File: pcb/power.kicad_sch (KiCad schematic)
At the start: 8 parts, among them Q1 AO3400A, Q2 AO3400A, U1 LM74610, U2 LM74610

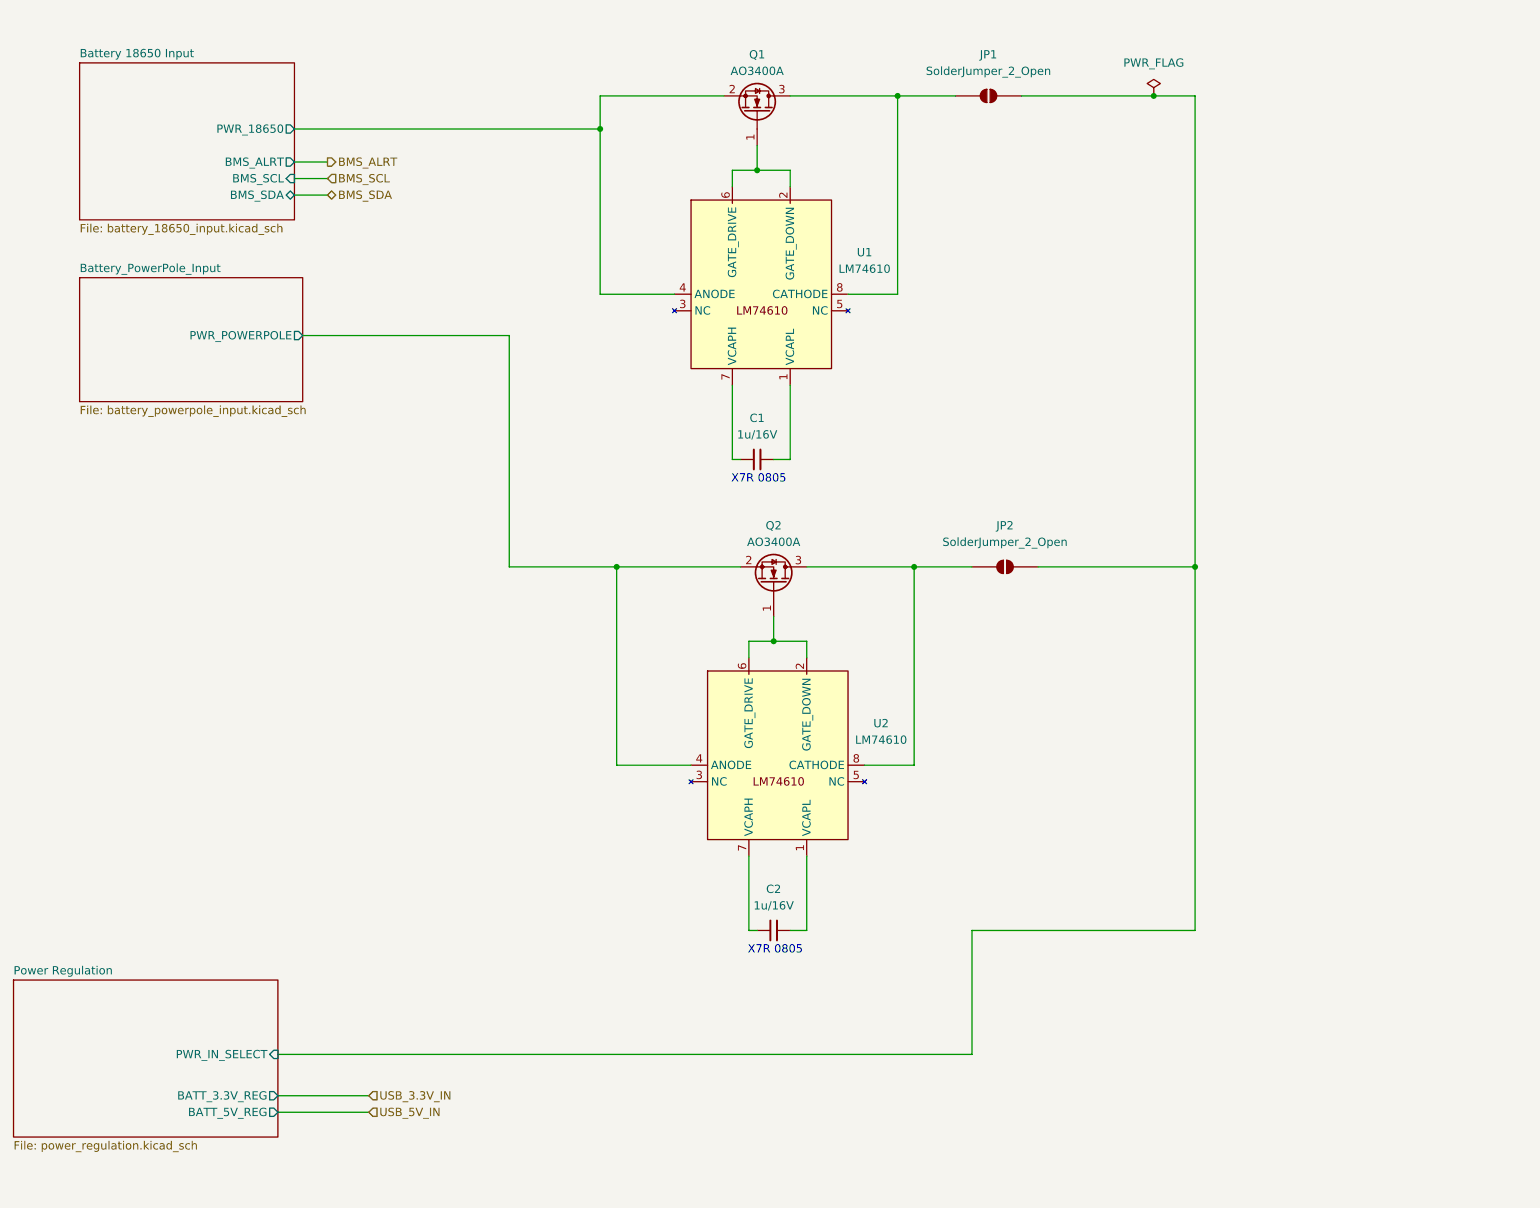
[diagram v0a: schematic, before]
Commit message: Replace battery/PowerPole ORing FETs with TPS2121 in VCOMP mode
power.kicad_sch: U12 (TPS2121RUXR) replaces the two LM74610+AO3400A ideal-
diode branches, configured per TI's "Highest Voltage Operation" (VCOMP,
Fig 10-15): PR1/CP2 tied to GND, OV1/OV2 resistor dividers (23.7k/5k) off
IN1 (PWR_18650) and IN2 (PWR_POWERPOLE), ILM set via R24 (51.1k), SS
ramped through C39 (0.01uF), ST tied directly to GND (unused). Divider
topology, ILM, and SS/ST wiring were each wrong on the first pass and
have been traced pin-by-pin and verified correct against the reference
schematic.

usbc-programming-uart.kicad_sch: CH340C VCC/V3 pin fix (VCC now correctly
powered from VBUS, V3 no longer driven externally) and F3 polyfuse
(16V/500mA) added in series on VBUS upstream of the hub/CH340/AMS1117.

battery_18650_input.kicad_sch, foxhunt1.kicad_pro: incidental KiCad
save cleanup (unused symbol-cache entry pruned, two collinear wire
segments merged, designator bookkeeping reordered) -- no circuit changes.

Bumps kicad_gx_library for the new TPS2121RUXR part. Adds
_docs/hardware/usb_battery_power_mux.md documenting the planned
3-stage TPS2121 architecture (this commit implements stage 1; stages
2/3, the USB-vs-regulator muxes, are not yet implemented).

Co-Authored-By: Claude Sonnet 5 <noreply@anthropic.com>
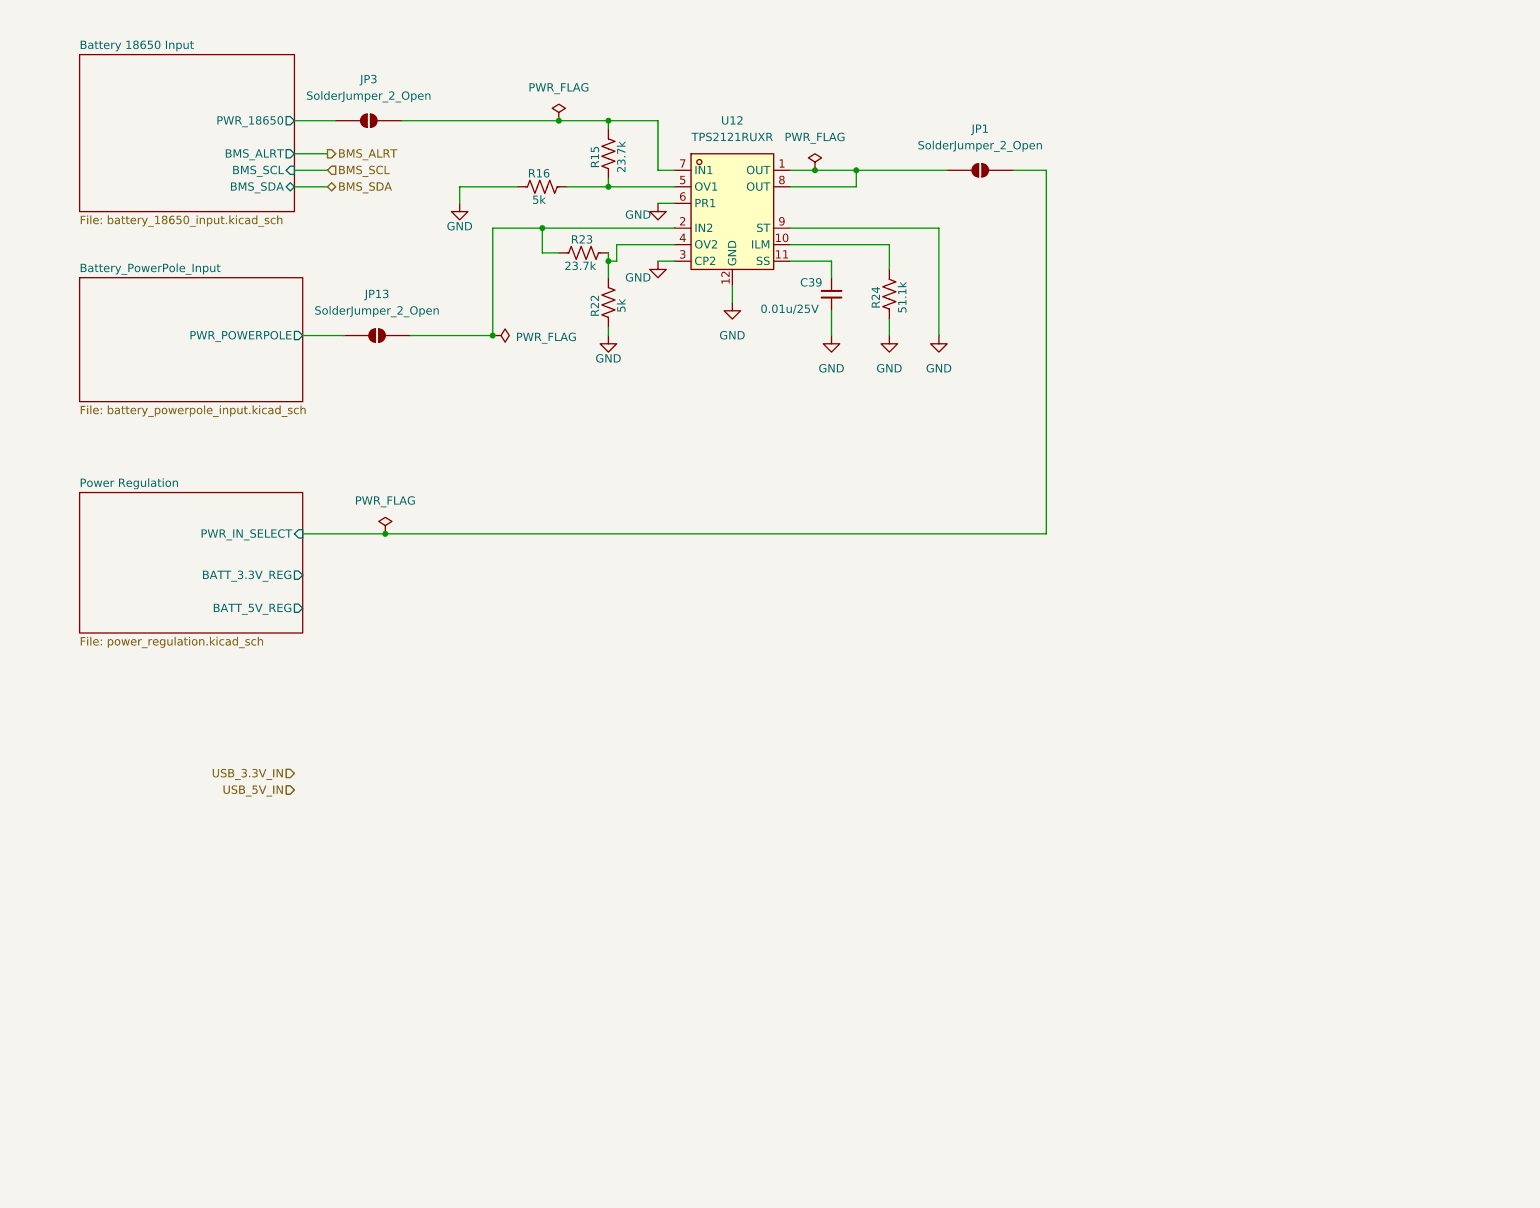
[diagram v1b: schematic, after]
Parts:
- removed C1, C2: 1u/16V, Capacitor_SMD:C_0805_2012Metric, symbol Device:C_Small
- removed JP2: SolderJumper_2_Open, Jumper:SolderJumper-2_P1.3mm_Open_TrianglePad1.0x1.5mm, symbol Jumper:SolderJumper_2_Open
- removed Q1, Q2: AO3400A, Package_TO_SOT_SMD:SOT-23, symbol Transistor_FET:AO3400A
- removed U1, U2: LM74610, Package_SO:VSSOP-8_3x3mm_P0.65mm, symbol kicad_gx_library:LM74610
- added C39: 0.01u/25V, Capacitor_SMD:C_0603_1608Metric, symbol Device:C_Small
- added JP13, JP3: SolderJumper_2_Open, Jumper:SolderJumper-2_P1.3mm_Open_TrianglePad1.0x1.5mm, symbol Jumper:SolderJumper_2_Open
- added R15, R23: 23.7k, Resistor_SMD:R_0603_1608Metric, symbol PCM_SparkFun-Resistor:R
- added R16, R22: 5k, Resistor_SMD:R_0201_0603Metric, symbol PCM_SparkFun-Resistor:R
- added R24: 51.1k, Resistor_SMD:R_0201_0603Metric, symbol PCM_SparkFun-Resistor:R
- added U12: TPS2121RUXR, kicad_gx_library:VQFN-HR-12_L2.5-W2.0-P0.50-BL, symbol kicad_gx_library:TPS2121RUXR
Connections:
- net Battery 18650 Input/PWR_18650: now also JP3.1 (A)
- net Battery_PowerPole_Input/PWR_POWERPOLE: now also JP13.1 (A)
- net at JP1.1 (A): now also U12.1 (OUT), U12.8 (OUT)
- new net: R22.1, R23.2, U12.4 (OV2)
- new net: R15.2, R16.1, U12.5 (OV1)
- new net: JP3.2 (B), R15.1, U12.7 (IN1)
- new net: R24.1, U12.10 (ILM)
- new net: C39.1, U12.11 (SS)
- new net: JP13.2 (B), R23.1, U12.2 (IN2)
- new net GND: C39.2, R16.2, R22.2, R24.2, U12.12 (GND), U12.3 (CP2), U12.6 (PR1), U12.9 (ST)
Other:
- note removed: "X7R 0805"
- moved on the sheet: JP1

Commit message: Add TPS2121 Stage 2/3: USB-vs-battery priority muxing on 5V and 3.3V rails
power.kicad_sch:
- U14 (TPS2121RUXR): 5V rail mux. IN1=BATT_5V_REG (priority), IN2=USB_5V_IN,
  OUT=+5V. PR1 tied to IN1, CP2/OV1/OV2 to GND (VREF priority mode -- battery
  always wins when present, no voltage-comparison ambiguity between two
  nominally-5V sources). ILM set via R26 (30.1k, ~3.5A class, sized with
  margin above the 2A SA818 budget for TX current transients). SS via C42
  (0.01uF). ST feeds the battery/USB detect logic below.
- U13 (TPS2121RUXR): 3.3V rail mux, same configuration. IN1=BATT_3.3V_REG,
  IN2=USB_3.3V_IN, OUT=+3.3V. ILM via R25 (80.6k, ~1.5A class, vs 1A
  peripheral budget). SS via C41.
- U1 (74LVC1G08): AND-gates U13.ST and U14.ST (each pulled up individually
  via R27/R28, 10k to +3.3V, since ST is open-drain) into PWR_ON_BATTERY --
  high only when both rails are confirmed running from battery, low if
  either has fallen back to USB. Output exposed as a new Power sheet pin.

foxhunt1.kicad_sch: bridges PWR_ON_BATTERY (Power sheet) to the new
IO_IN_ON_BATT input on the mcu-esp32 sheet, and USB_3.3V_IN/USB_5V_IN
(Power sheet) to USB_3.3V/USB_5V (USB-C sheet) -- these were previously
unconnected placeholder labels.

mcu-esp32.kicad_sch: IO_IN_ON_BATT wired to U8 pin 35 (GPIO42), the one
GPIO the pinout doc had marked as still spare.

kicad_gx_library: TPS2121RUXR symbol fix (one OUT pin marked passive
instead of output, since the two physical OUT pins are meant to be tied
together -- avoids an ERC driver-conflict false positive).

power_regulation.kicad_sch, battery_18650_input.kicad_sch,
battery_powerpole_input.kicad_sch, foxhunt1.kicad_pro: incidental KiCad
save cleanup, no circuit changes (verified via orphan/short checks and
netlist diff -- same components as before).

Fully traced pin-by-pin: both mux dividers/ILM/SS wiring, the battery-vs-
USB source assignment on each rail (not swapped), the AND-gate inputs,
and all three cross-sheet bridges. 0 new orpha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
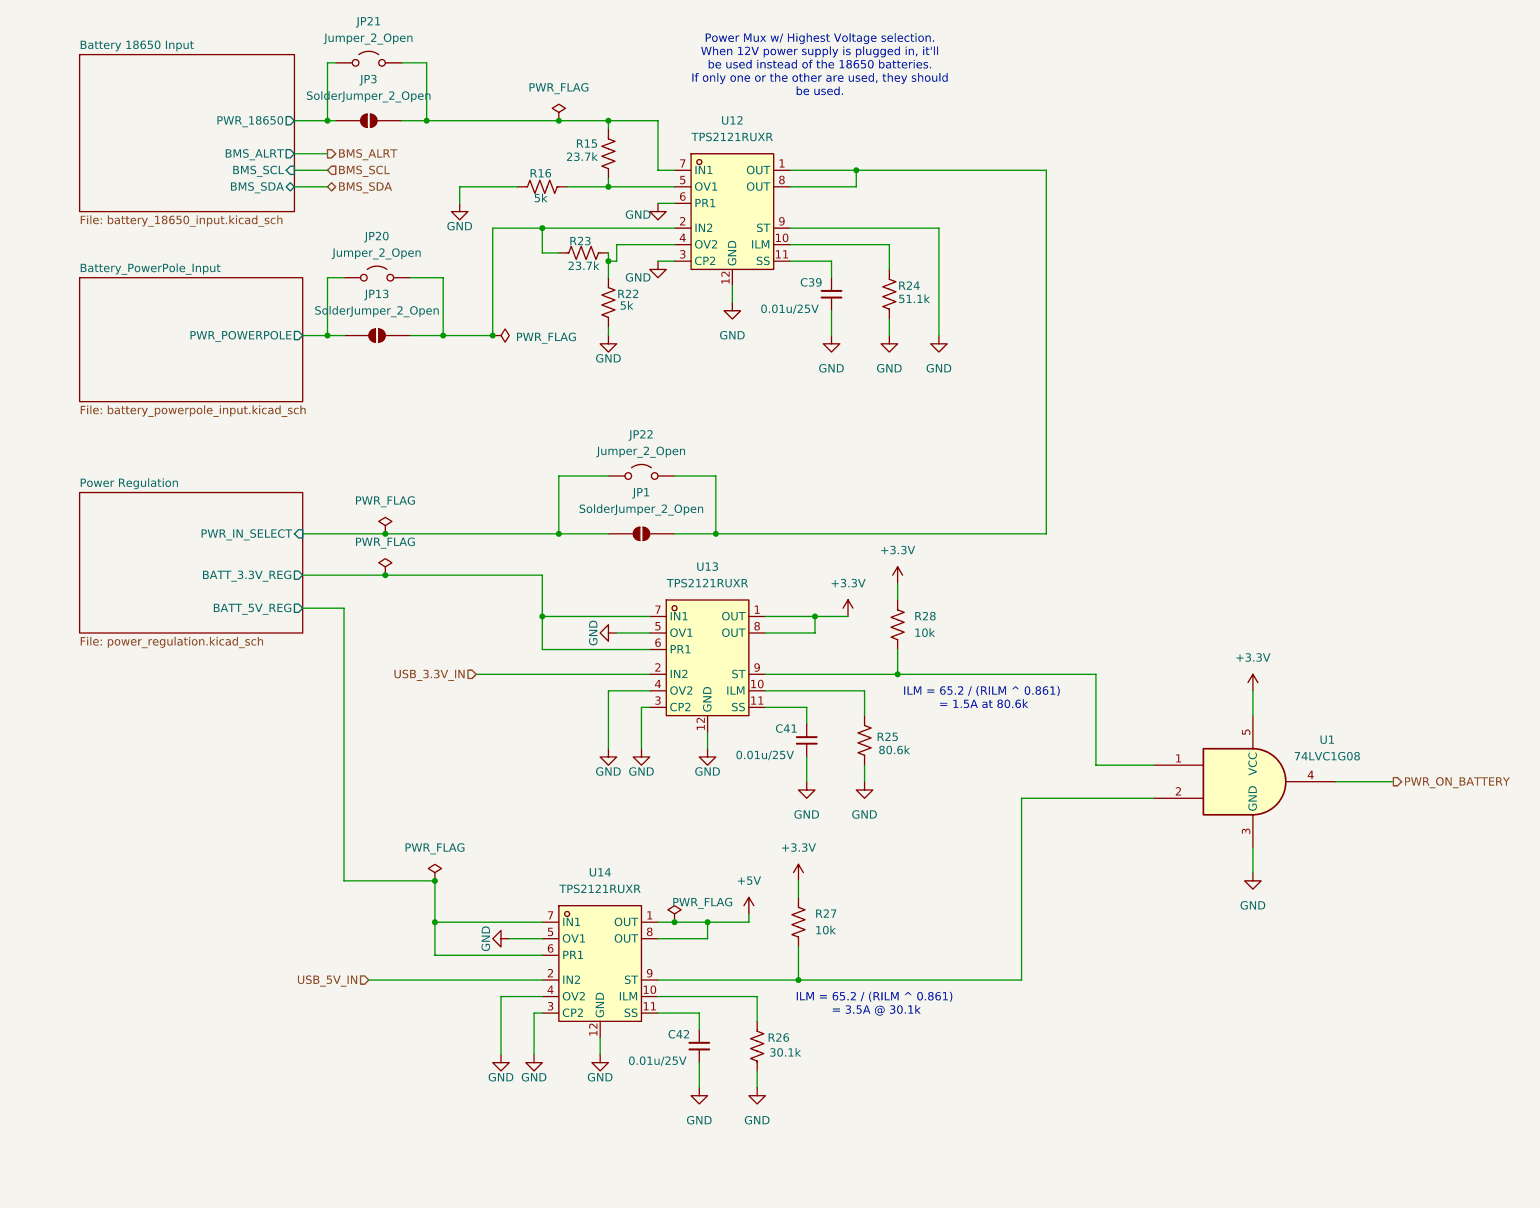
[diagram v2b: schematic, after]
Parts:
- added C41, C42: 0.01u/25V, Capacitor_SMD:C_0603_1608Metric, symbol Device:C_Small
- added JP20, JP21, JP22: Jumper_2_Open, symbol Jumper:Jumper_2_Open
- added R25: 80.6k, Resistor_SMD:R_0201_0603Metric, symbol Device:R_US
- added R26: 30.1k, Resistor_SMD:R_0201_0603Metric, symbol Device:R_US
- added R27, R28: 10k, Resistor_SMD:R_0805_2012Metric, symbol Device:R_US
- added U1: 74LVC1G08, Package_TO_SOT_SMD:SOT-23-5, symbol 74xGxx:74LVC1G08
- added U13, U14: TPS2121RUXR, kicad_gx_library:VQFN-HR-12_L2.5-W2.0-P0.50-BL, symbol kicad_gx_library:TPS2121RUXR
- R15, R16, R22, R23, R24: symbol PCM_SparkFun-Resistor:R -> Device:R_US
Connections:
- net Battery 18650 Input/PWR_18650: now also JP21.1 (A)
- net Battery_PowerPole_Input/PWR_POWERPOLE: now also JP20.1 (A)
- net GND: now also R16.1, R22.1, R24.1, C41.2, C42.2, R25.1, R26.1, U1.3 (GND), U13.12 (GND), U13.3 (CP2), U13.4 (OV2), U13.5 (OV1), U14.12 (GND), U14.3 (CP2), U14.4 (OV2), U14.5 (OV1); no longer R16.2, R22.2, R24.2
- net Power Regulation/BATT_3.3V_REG: now also U13.6 (PR1), U13.7 (IN1)
- net Power Regulation/BATT_5V_REG: now also U14.6 (PR1), U14.7 (IN1)
- net Power Regulation/PWR_IN_SELECT: now also JP1.1 (A), JP22.1 (A); no longer JP1.2 (B)
- net USB_3.3V_IN: now also U13.2 (IN2)
- net USB_5V_IN: now also U14.2 (IN2)
- net at JP3.2 (B), U12.7 (IN1): now also R15.2, JP21.2 (B); no longer R15.1
- net at U12.1 (OUT), U12.8 (OUT): now also JP1.2 (B), JP22.2 (B); no longer JP1.1 (A)
- net at U12.10 (ILM): now also R24.2; no longer R24.1
- net at JP13.2 (B), U12.2 (IN2): now also R23.2, JP20.2 (B); no longer R23.1
- new net: R22.2, R23.1, U12.4 (OV2)
- new net: R15.1, R16.2, U12.5 (OV1)
- new net: C41.1, U13.11 (SS)
- new net: R26.2, U14.10 (ILM)
- new net: R27.1, U1.2, U14.9 (ST)
- new net: C42.1, U14.11 (SS)
- new net: R28.1, U1.1, U13.9 (ST)
- new net: R25.2, U13.10 (ILM)
- new net +3.3V: R27.2, R28.2, U1.5 (VCC), U13.1 (OUT), U13.8 (OUT)
- new net +5V: U14.1 (OUT), U14.8 (OUT)
- new net PWR_ON_BATTERY: U1.4
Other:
- note added: "ILM = 65.2 / (RILM ^ 0.861) = 1.5A at 80.6k"
- note added: "ILM = 65.2 / (RILM ^ 0.861) = 3.5A @ 30.1k"
- note added: "Power Mux w/ Highest Voltage selection. When 12V power supply is plugged in, it'll be used instead of the 18650 batteries. If only one or the other are used, they should be used."
- moved on the sheet: R15, R16, R22, R23, R24
